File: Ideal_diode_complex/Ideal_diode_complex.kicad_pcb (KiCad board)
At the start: 2 copper layers, 0 parts

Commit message: Finished complex ideal diode PCB
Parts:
- added C1: 100 nF, Capacitor_SMD:C_0603_1608Metric, F.Cu at (103.5, 102.5)
- added C2: 100 nF, Capacitor_SMD:C_0603_1608Metric, F.Cu at (103.0, 93.5)
- added C3: 10 uF, Capacitor_SMD:C_1206_3216Metric, F.Cu at (98.0, 90.5)
- added CN1: 24_243_1, JLCImport:24_243_1, F.Cu at (83.7, 88.7)
- added CN2: 24_243_1, JLCImport:24_243_1, F.Cu at (126.5, 89.0)
- added CN3: 24_243_2, JLCImport:24_243_2, F.Cu at (83.7, 106.0)
- added CN4: 24_243_2, JLCImport:24_243_2, F.Cu at (126.3, 106.8)
- added D1: PMEG2010ER_115, JLCImport:PMEG2010ER_115, F.Cu at (111.5, 114.0)
- added H1: MountingHole, MountingHole:MountingHole_2.7mm_M2.5, F.Cu at (136.0, 78.0)
- added H2: MountingHole, MountingHole:MountingHole_2.7mm_M2.5, F.Cu at (136.0, 120.0)
- added H3: MountingHole, MountingHole:MountingHole_2.7mm_M2.5, F.Cu at (74.0, 120.0)
- added H4: MountingHole, MountingHole:MountingHole_2.7mm_M2.5, F.Cu at (74.0, 78.0)
- added LED1: 0805G_Green, JLCImport:0805G_Green, F.Cu at (103.9, 110.0)
- added LED2: FC-2012HRK-620D, JLCImport:FC-2012HRK-620D, F.Cu at (104.0, 114.0)
- added Q1: SI7336ADP-T1-GE3-HXY, JLCImport:SI7336ADP-T1-GE3-HXY, F.Cu at (106.8, 89.0)
- added R1: 2.7k, Resistor_SMD:R_0805_2012Metric, F.Cu at (99.5, 114.0)
- added R2: 2.7k, Resistor_SMD:R_0805_2012Metric, F.Cu at (99.6, 110.0)
- added TP1: TestPoint, TestPoint:TestPoint_Pad_D1.0mm, F.Cu at (95.5, 116.5)
- added TP2: TestPoint, TestPoint:TestPoint_Pad_D1.0mm, F.Cu at (129.0, 117.5)
- added TP3: TestPoint, TestPoint:TestPoint_Pad_D1.0mm, F.Cu at (112.0, 81.0)
- added TP4: TestPoint, TestPoint:TestPoint_Pad_D1.0mm, F.Cu at (106.5, 81.0)
- added TP5: TestPoint, TestPoint:TestPoint_Pad_D1.0mm, F.Cu at (98.0, 81.0)
- added U2: LTC4352CMS_TRPBF, JLCImport:LTC4352CMS_TRPBF, F.Cu at (104.1, 98.0)
- added USB2: 10118194-0001LF, JLCImport:10118194-0001LF, F.Cu at (122.5, 119.4)
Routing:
- net GND: track 0.00 -> 99.2 mm
- net Net-(U2-SOURCE): track 0.00 -> 60.7 mm
- net Net-(D1-C): track 0.00 -> 44.9 mm, vias 0 -> 2
- net Net-(Q1-D): track 0.00 -> 44.2 mm, vias 0 -> 2
- net Net-(Q1-G): track 0.00 -> 20.9 mm, vias 0 -> 2
- net Net-(LED2--): track 0.00 -> 18.0 mm, vias 0 -> 2
- net Net-(LED1-K): track 0.00 -> 12.7 mm, vias 0 -> 2
- net Net-(D1-A): track 0.00 -> 11.0 mm
- net Net-(LED2-+): track 0.00 -> 2.50 mm
- net Net-(LED1-A): track 0.00 -> 2.35 mm
- net Net-(U2-CPO): track 0.00 -> 2.34 mm
- added copper zone on B.Cu, net GND
- added copper zone on F.Cu, net GND
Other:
- board outline added: 70 x 50 mm
- board text added: "GATE"
- board text added: "GND"
- board text added: "INPUT"
- board text added: "OUTPUT"
- board text added: "VCC"
- board text added: "Vin"
- board text added: "Vout"

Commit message: minor updates
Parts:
- moved USB2 0.50 mm to (122.5, 118.9)
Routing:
- net GND: track 99.2 -> 89.0 mm

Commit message: Added a boost converter to the USB line to make sure VCC stays above 4.7V
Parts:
- removed USB2: 10118194-0001LF, JLCImport:10118194-0001LF
- added C4: 10 uF, Capacitor_SMD:C_0402_1005Metric, F.Cu at (111.5, 113.0)
- added C5: 10 uF, Capacitor_SMD:C_0402_1005Metric, F.Cu at (106.5, 113.5)
- added C6: 10 uF, Capacitor_SMD:C_0402_1005Metric, F.Cu at (107.5, 113.5)
- added C7: 10 uF, Capacitor_SMD:C_0402_1005Metric, F.Cu at (105.5, 113.5)
- added L1: VLS201610HBX-2R2M-1, JLCImport:VLS201610HBX-2R2M-1, F.Cu at (113.5, 114.0)
- added R3: 5.1 k, Resistor_SMD:R_0402_1005Metric, F.Cu at (121.0, 115.0)
- added R4: 5.1 k, Resistor_SMD:R_0402_1005Metric, F.Cu at (122.0, 115.0)
- added R5: 51k, Resistor_SMD:R_0402_1005Metric, F.Cu at (107.5, 115.5)
- added R6: 12k, Resistor_SMD:R_0402_1005Metric, F.Cu at (107.5, 117.5)
- added U1: TPS61099DRVR, JLCImport:TPS61099DRVR, F.Cu at (109.5, 115.0)
- added USB1: TYPE-C_6P, JLCImport:TYPE-C_6P, F.Cu at (121.5, 119.0)
- C1, C2: footprint Capacitor_SMD:C_0603_1608Metric -> Capacitor_SMD:C_0402_1005Metric
- LED1: value 0805G_Green -> 0603White_light_C2290; footprint JLCImport:0805G_Green -> JLCImport:0603White_light_C2290
- LED2: value FC-2012HRK-620D -> KT-0603R; footprint JLCImport:FC-2012HRK-620D -> JLCImport:KT-0603R
- R1, R2: footprint Resistor_SMD:R_0805_2012Metric -> Resistor_SMD:R_0603_1608Metric
- moved TP2 20.6 mm to (110.0, 109.5)
- moved D1 13.0 mm to (98.5, 115.0), turned to 0 degrees
- moved LED2 3.20 mm to (102.0, 111.5)
- moved R1 2.69 mm to (98.5, 111.5)
- moved LED1 2.19 mm to (102.0, 109.0)
- moved TP1 2.00 mm to (93.5, 116.5)
- moved R2 1.51 mm to (98.5, 109.0)
- moved C1 0.50 mm to (103.5, 102.0)
- moved C2 0.50 mm to (103.0, 94.0)
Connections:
- net Net-(Q1-D) renamed /CELL +
- net Net-(U2-SOURCE) renamed /PSU +
- LED2 pad 1: Net-(LED2--) -> Net-(LED2-A)
- LED2 pad 2: Net-(LED2-+) -> Net-(LED2-K)
- R1 pad 1: Net-(LED2-+) -> Net-(LED2-A)
- U2 pad 6: Net-(LED2--) -> Net-(LED2-K)
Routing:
- net /AUX 5V: track 0.00 -> 24.1 mm, vias 0 -> 2
- net Net-(LED2--): track 18.0 -> 0.00 mm, vias 2 -> 0
- net GND: track 89.0 -> 104.9 mm, vias 0 -> 2
- net Net-(LED2-K): track 0.00 -> 14.8 mm, vias 0 -> 2
- net Net-(D1-C): track 44.9 -> 31.5 mm
- net Net-(U1-SW): track 0.00 -> 3.25 mm
- net Net-(LED2-+): track 2.50 -> 0.00 mm
- net Net-(U1-FB): track 0.00 -> 2.11 mm
- net Net-(LED2-A): track 0.00 -> 1.92 mm
- net Net-(LED1-K): track 12.7 -> 11.1 mm
- net Net-(D1-A): track 11.2 -> 9.72 mm
- net Net-(USB1-CC2): track 0.00 -> 1.46 mm
- net Net-(USB1-CC1): track 0.00 -> 1.46 mm
- net /PSU +: track 60.7 -> 60.1 mm

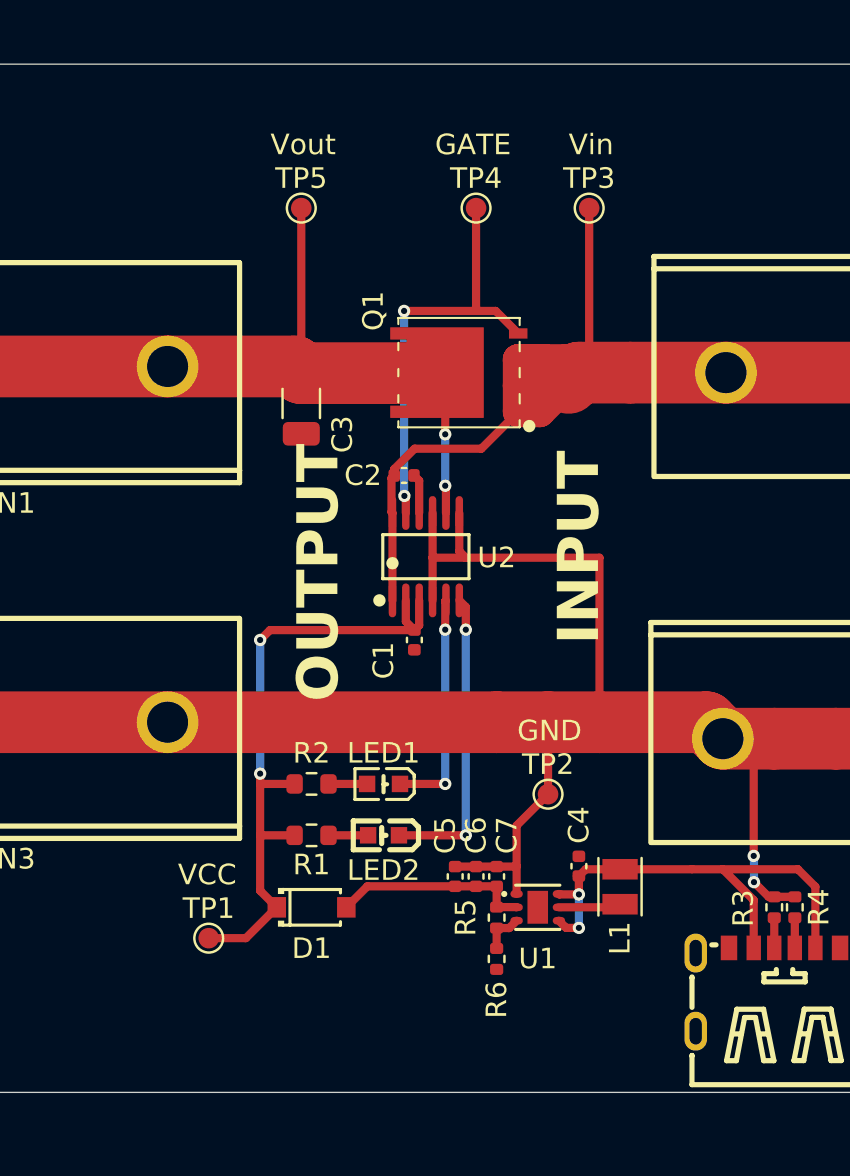
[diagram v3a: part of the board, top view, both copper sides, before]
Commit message: updated to use different voltage regulator smd to be cheaper
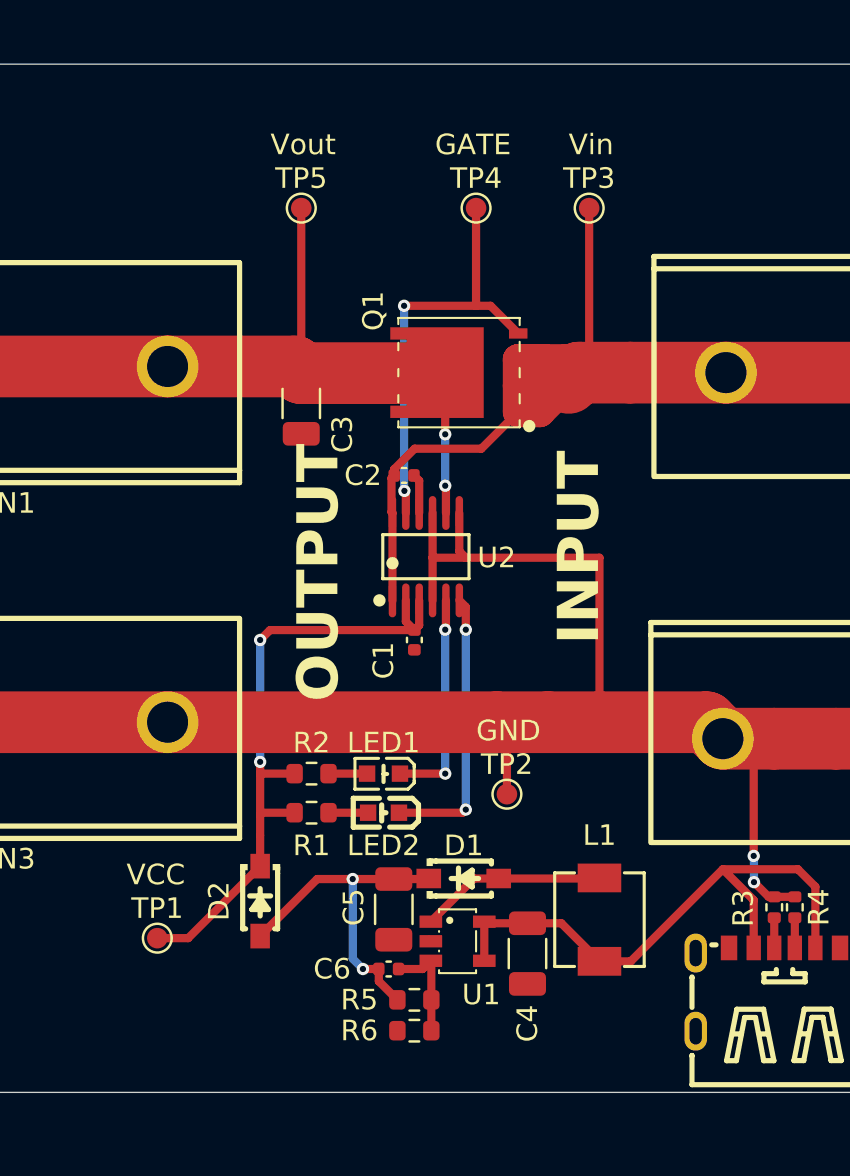
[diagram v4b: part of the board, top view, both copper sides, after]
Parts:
- removed C7: 10 uF, Capacitor_SMD:C_0402_1005Metric
- added D2: B5819W_C8598, JLCImport:B5819W_C8598, F.Cu at (96.0, 114.7)
- C4: value 10 uF -> 22 uF; footprint Capacitor_SMD:C_0402_1005Metric -> Capacitor_SMD:C_1206_3216Metric
- C5: value 10 uF -> 47 uF; footprint Capacitor_SMD:C_0402_1005Metric -> Capacitor_SMD:C_1206_3216Metric
- C6: value 10 uF -> 10 nF
- D1: value PMEG2010ER_115 -> B5819W_C8598; footprint JLCImport:PMEG2010ER_115 -> JLCImport:B5819W_C8598
- L1: value VLS201610HBX-2R2M-1 -> MWSA0402S-100MT; footprint JLCImport:VLS201610HBX-2R2M-1 -> JLCImport:MWSA0402S-100MT
- R1, R2: value 2.7k -> 2.7 k
- R5: value 51k -> 18 k; footprint Resistor_SMD:R_0402_1005Metric -> Resistor_SMD:R_0603_1608Metric
- R6: value 12k -> 5.1 k; footprint Resistor_SMD:R_0402_1005Metric -> Resistor_SMD:R_0603_1608Metric
- U1: value TPS61099DRVR -> TPS61041DBVR; footprint JLCImport:TPS61099DRVR -> JLCImport:TPS61041DBVR
- moved D1 7.53 mm to (105.9, 113.6)
- moved C6 6.91 mm to (102.2, 118.0), turned to 0 degrees
- moved R5 5.66 mm to (103.5, 119.5), turned to 0 degrees
- moved R6 5.31 mm to (103.5, 121.0), turned to 180 degrees
- moved C4 4.93 mm to (109.0, 117.2), turned to -90 degrees
- moved C5 4.31 mm to (102.5, 115.1)
- moved U1 4.23 mm to (105.6, 116.6), turned to 180 degrees
- moved TP1 2.50 mm to (91.0, 116.5)
- moved TP2 2.00 mm to (108.0, 109.5)
- moved L1 1.89 mm to (112.5, 115.6)
- moved LED2 1.10 mm to (102.0, 110.4)
- moved R1 1.10 mm to (98.5, 110.4)
- moved LED1 0.50 mm to (102.0, 108.5)
- moved R2 0.50 mm to (98.5, 108.5)
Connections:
- C1 pad 1: Net-(D1-C) -> Net-(D2--)
- C4 pad 1: /AUX 5V -> Net-(U1-EN)
- C5 pad 1: Net-(D1-A) -> GND
- C5 pad 2: GND -> Net-(D1--)
- C6 pad 1: Net-(D1-A) -> Net-(D1--)
- C6 pad 2: GND -> Net-(U1-FB)
- D1 pad 1: Net-(D1-C) -> Net-(D1--)
- D1 pad 2: Net-(D1-A) -> Net-(D1-+)
- L1 pad 1: /AUX 5V -> Net-(U1-EN)
- L1 pad 2: Net-(U1-SW) -> Net-(D1-+)
- R1 pad 2: Net-(D1-C) -> Net-(D2--)
- R2 pad 2: Net-(D1-C) -> Net-(D2--)
- R5 pad 1: Net-(U1-FB) -> Net-(D1--)
- R5 pad 2: Net-(D1-A) -> Net-(U1-FB)
- R6 pad 1: GND -> Net-(U1-FB)
- R6 pad 2: Net-(U1-FB) -> GND
- TP1 pad 1: Net-(D1-C) -> Net-(D2--)
- U1 pad 1: GND -> Net-(D1-+)
- U1 pad 2: Net-(D1-A) -> GND
- U1 pad 4: /AUX 5V -> Net-(U1-EN)
- U1 pad 5: Net-(U1-SW) -> Net-(U1-EN)
- U2 pad 2: Net-(D1-C) -> Net-(D2--)
- U2 pad 3: Net-(D1-C) -> Net-(D2--)
- USB1 pad A9: /AUX 5V -> Net-(U1-EN)
- USB1 pad B9: /AUX 5V -> Net-(U1-EN)
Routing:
- net Net-(D2--): track 0.00 -> 31.7 mm, vias 0 -> 2
- net Net-(D1-C): track 31.5 -> 0.00 mm, vias 2 -> 0
- net Net-(U1-EN): track 0.00 -> 28.4 mm
- net /AUX 5V: track 24.1 -> 0.00 mm, vias 2 -> 0
- net Net-(D1--): track 0.00 -> 16.6 mm, vias 0 -> 2
- net Net-(D1-A): track 9.72 -> 0.00 mm
- net GND: track 104.9 -> 95.4 mm
- net Net-(D1-+): track 0.00 -> 9.08 mm
- net Net-(U1-SW): track 3.25 -> 0.00 mm
- net Net-(U1-FB): track 2.11 -> 5.15 mm
- net Net-(LED2-K): track 14.8 -> 13.6 mm
- net Net-(LED1-K): track 11.1 -> 10.6 mm

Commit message: Final design
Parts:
- removed C5: 47 uF, Capacitor_SMD:C_1206_3216Metric
- removed C6: 10 nF, Capacitor_SMD:C_0402_1005Metric
- removed D1, D2: B5819W_C8598, JLCImport:B5819W_C8598
- removed L1: MWSA0402S-100MT, JLCImport:MWSA0402S-100MT
- removed R5: 18 k, Resistor_SMD:R_0603_1608Metric
- removed R6: 5.1 k, Resistor_SMD:R_0603_1608Metric
- added TP6: TestPoint, TestPoint:TestPoint_Pad_D1.0mm, F.Cu at (100.3, 119.0)
- C3: value 10 uF -> 1 uF; footprint Capacitor_SMD:C_1206_3216Metric -> Capacitor_SMD:C_0402_1005Metric
- C4: value 22 uF -> 1 uF; footprint Capacitor_SMD:C_1206_3216Metric -> Capacitor_SMD:C_0402_1005Metric
- U1: value TPS61041DBVR -> MAX40200AUK_T; footprint JLCImport:TPS61041DBVR -> JLCImport:MAX40200AUK_T
- moved C3 23.9 mm to (96.8, 114.4), turned to 90 degrees
- moved R3 11.7 mm to (109.5, 113.0)
- moved R4 11.7 mm to (110.5, 113.0)
- moved USB1 11.7 mm to (110.0, 117.0)
- moved C4 8.03 mm to (101.5, 114.4), turned to 90 degrees
- moved U1 7.44 mm to (99.1, 112.9), turned to 90 degrees
- moved TP2 4.42 mm to (111.2, 106.5)
- moved LED1 4.37 mm to (104.9, 105.2)
- moved LED2 4.37 mm to (104.9, 107.2)
- moved R1 4.37 mm to (101.4, 107.2)
- moved R2 4.37 mm to (101.4, 105.2)
- moved TP1 3.04 mm to (94.0, 117.0)
- moved H2 2.00 mm to (136.0, 118.0)
- moved H3 2.00 mm to (74.0, 118.0)
- moved CN1 0.80 mm to (82.8, 88.7)
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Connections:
- C1 pad 1: Net-(D2--) -> Net-(U1-OUT)
- C3 pad 1: /CELL + -> GND
- C3 pad 2: GND -> Net-(U1-OUT)
- C4 pad 1: Net-(U1-EN) -> GND
- C4 pad 2: GND -> Net-(U1-EN)
- R1 pad 2: Net-(D2--) -> Net-(U1-OUT)
- R2 pad 2: Net-(D2--) -> Net-(U1-OUT)
- TP1 pad 1: Net-(D2--) -> Net-(U1-OUT)
- U1 pad 1: Net-(D1-+) -> Net-(U1-EN)
- U1 pad 3: Net-(U1-FB) -> Net-(U1-EN)
- U1 pad 4: Net-(U1-EN) -> unconnected-(U1-N.C.-Pad4)
- U1 pad 5: Net-(U1-EN) -> Net-(U1-OUT)
- U2 pad 2: Net-(D2--) -> Net-(U1-OUT)
- U2 pad 3: Net-(D2--) -> Net-(U1-OUT)
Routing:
- net GND: track 95.4 -> 8.71 mm, vias 2 -> 640
- net Net-(D2--): track 31.7 -> 0.00 mm, vias 2 -> 0
- net Net-(U1-OUT): track 0.00 -> 24.5 mm
- net Net-(D1--): track 16.6 -> 0.00 mm, vias 2 -> 0
- net Net-(D1-+): track 9.08 -> 0.00 mm
- net /PSU +: track 60.1 -> 67.1 mm
- net Net-(U1-EN): track 28.4 -> 22.9 mm
- net Net-(U1-FB): track 5.15 -> 0.00 mm
- net Net-(LED2-K): track 13.6 -> 10.3 mm, vias 2 -> 0
- net Net-(LED1-K): track 10.6 -> 7.32 mm, vias 2 -> 0
- net /CELL +: track 44.2 -> 44.7 mm
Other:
- board size 70 x 50 mm -> 70 x 48 mm
- board text added: "Ideal Diode"
- board text added: "VUSB"
